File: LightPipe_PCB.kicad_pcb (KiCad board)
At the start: 4 copper layers, 38 x 38 mm, 15 parts, among them J5 AudioJack4, M1 2.2mm_M2, M2 2.2mm_M2, X1 KLB-4, X2 KLB-4, X3 XT30, X4.1 Cable-0.7mm, X4.2 Cable-0.7mm, X5.1 Cable-1.5mm, X5.2 Cable-1.5mm

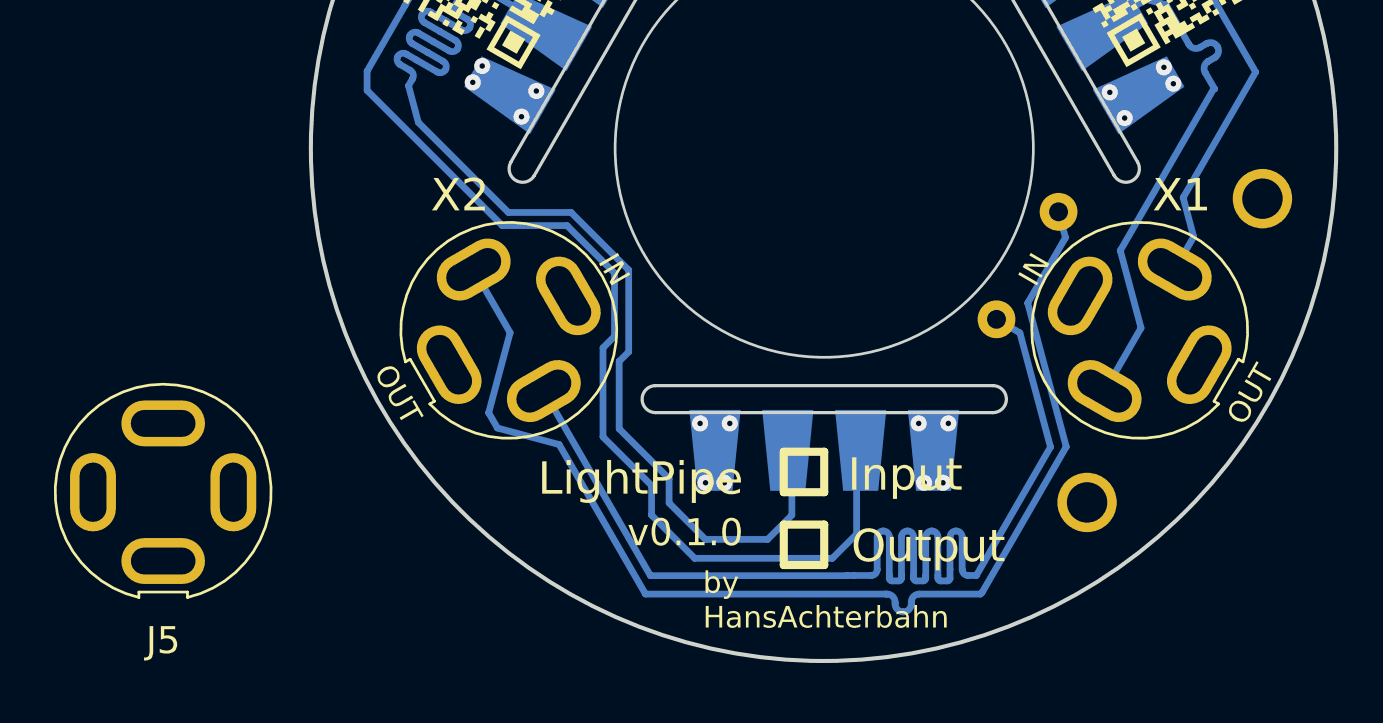
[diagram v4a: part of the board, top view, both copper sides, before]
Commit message: [clean] improved schematic and pcb to be easier to read in Input-Mode 2
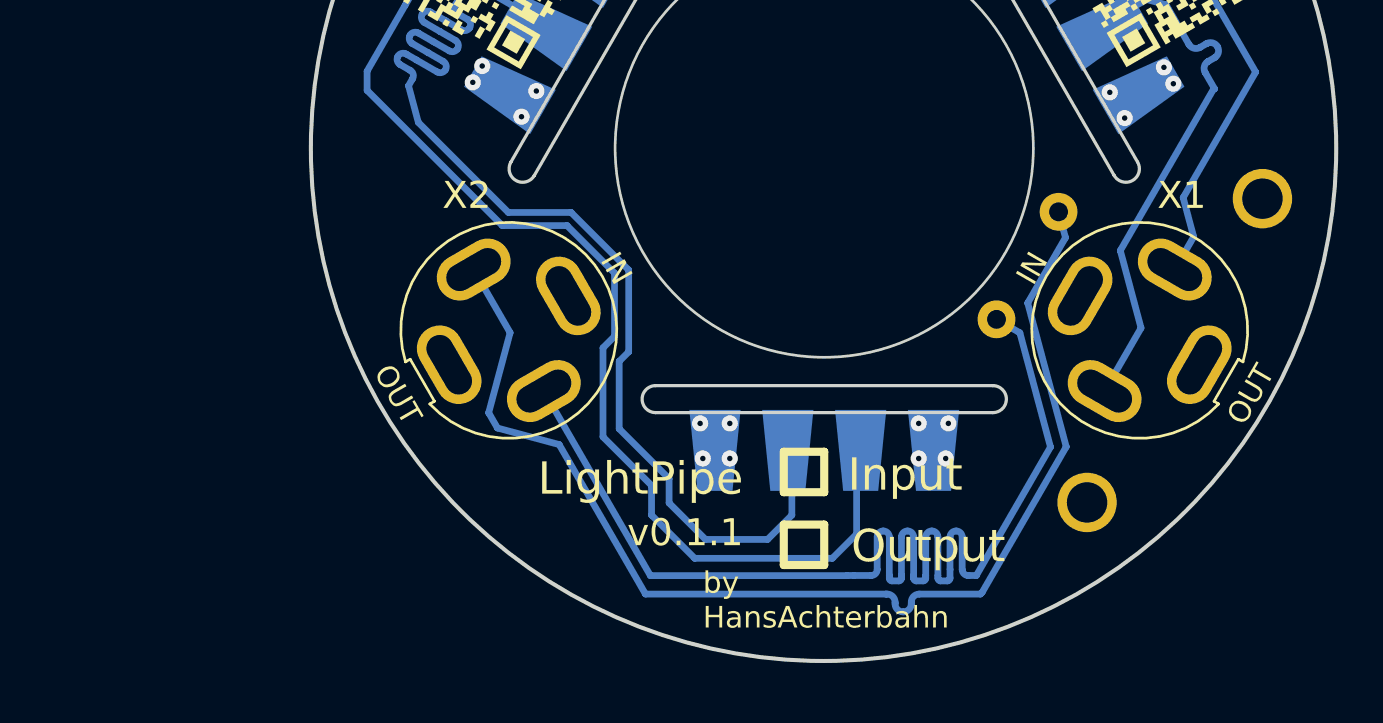
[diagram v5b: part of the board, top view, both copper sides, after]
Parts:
- removed J5: AudioJack4, h8-Connectors:Lumberg-KLB-4-Klinkensteckverbinder-3_5-180deg-turnable
- X1, X2: value KLB-4 -> AudioJack4; footprint h8-Connectors:Lumberg-KLB-4-Klinkensteckverbinder-3_5-180deg-turnable -> h8-Connectors:Lumberg-KLB-4-Jack-3_5-180deg-turnable
- renumbered X4.2 to X4.1, X4.1 to X4.2
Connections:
- X4.1 pad 1: /d3 -> /clk3
- X4.2 pad 1: /clk3 -> /d3
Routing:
- net /clk1: track 0.00 -> 20.0 mm
- net /d1: track 39.9 -> 20.0 mm
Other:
- board text added: "${REVISION}"
- board text added: "by ${COMPANY}"
- board text removed: "by HansAchterbahn"
- board text removed: "v0.1.0"
